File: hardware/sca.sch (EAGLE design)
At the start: 64 parts, among them IC1 BMP388, Q1 BSS138, Q2 BSS138, Q3 2N7002D, U1 MIC5225-3.3, U2 MIC5225-3.3, U5 FGPMMOPA6H, U6 MIC5225-3.3, Y1 32.768kHz

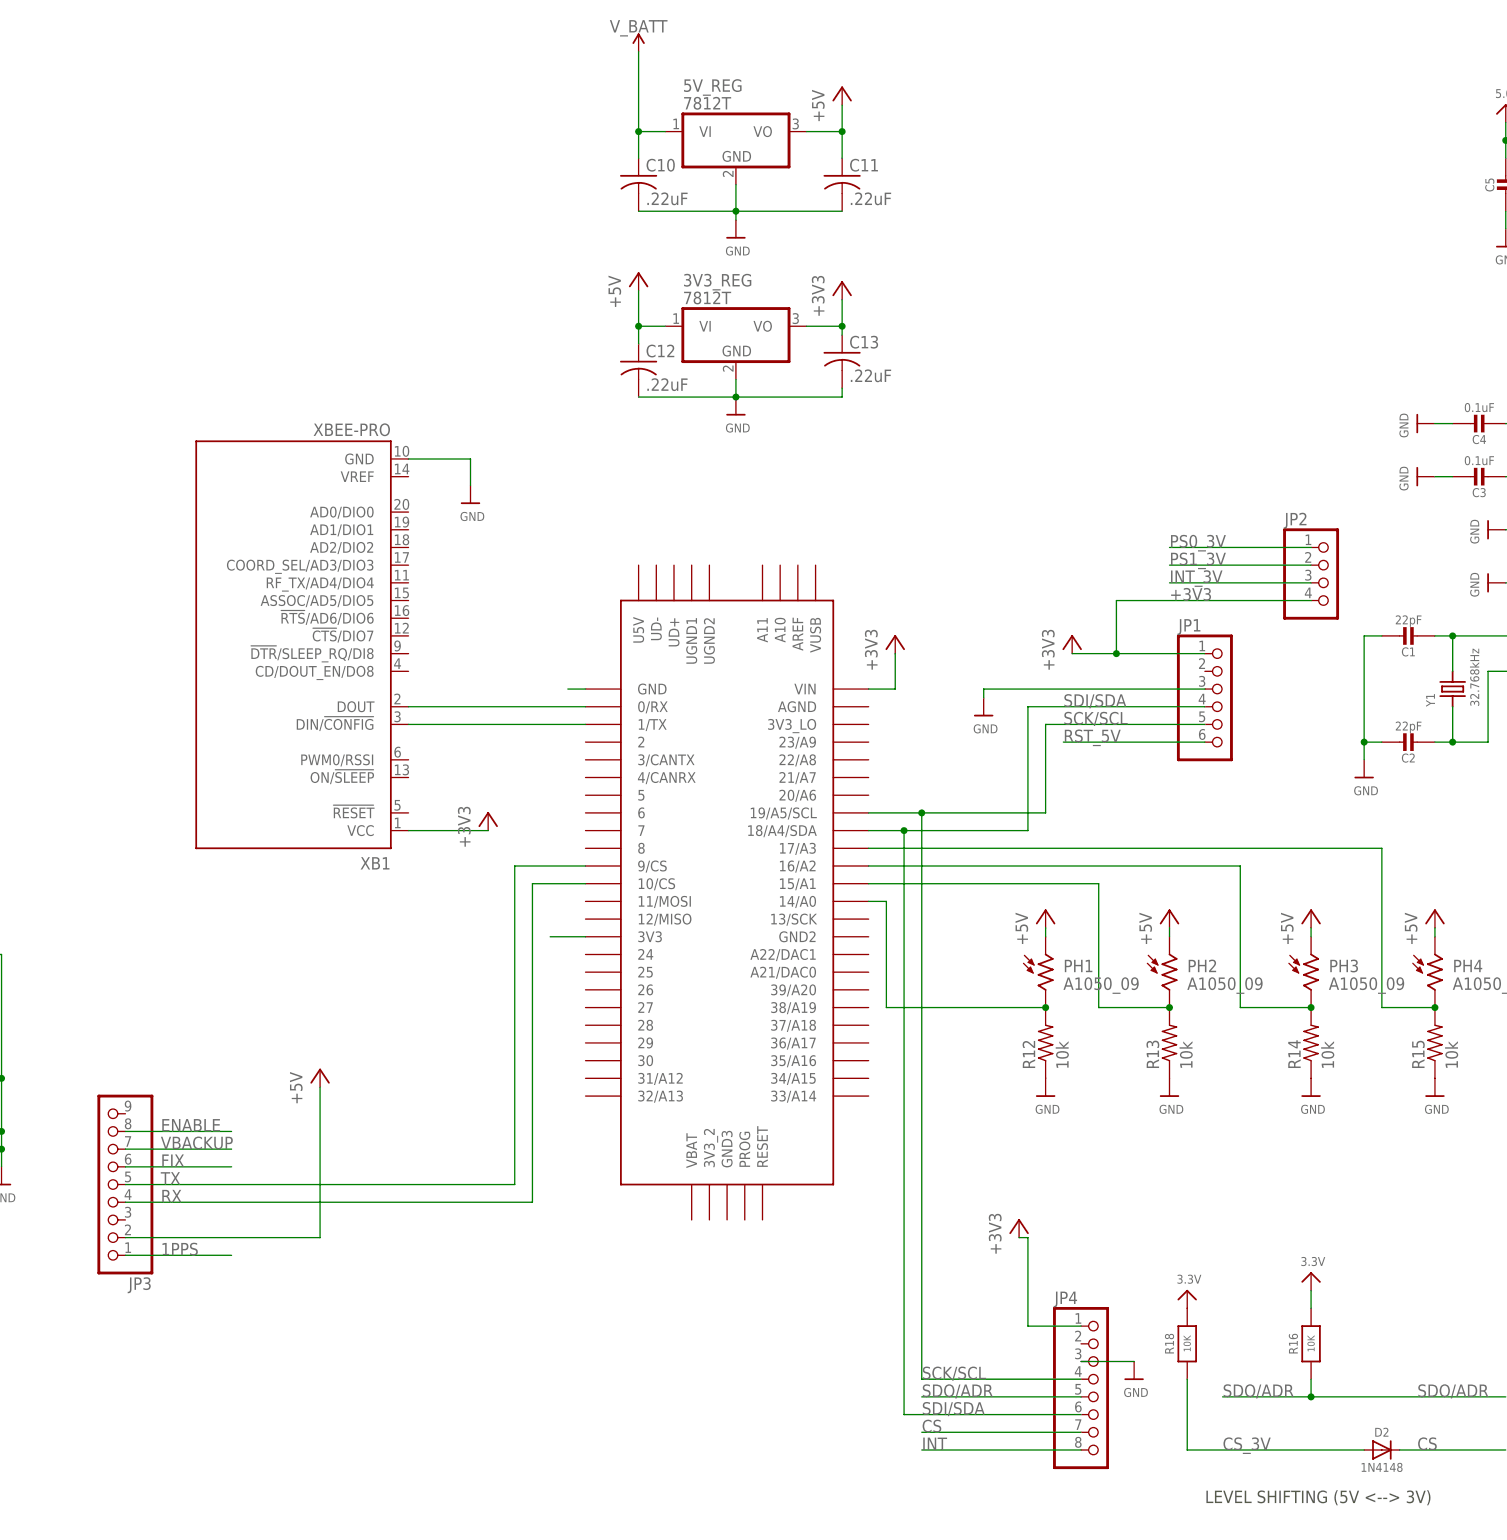
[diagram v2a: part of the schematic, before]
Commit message: added thermistor circuit
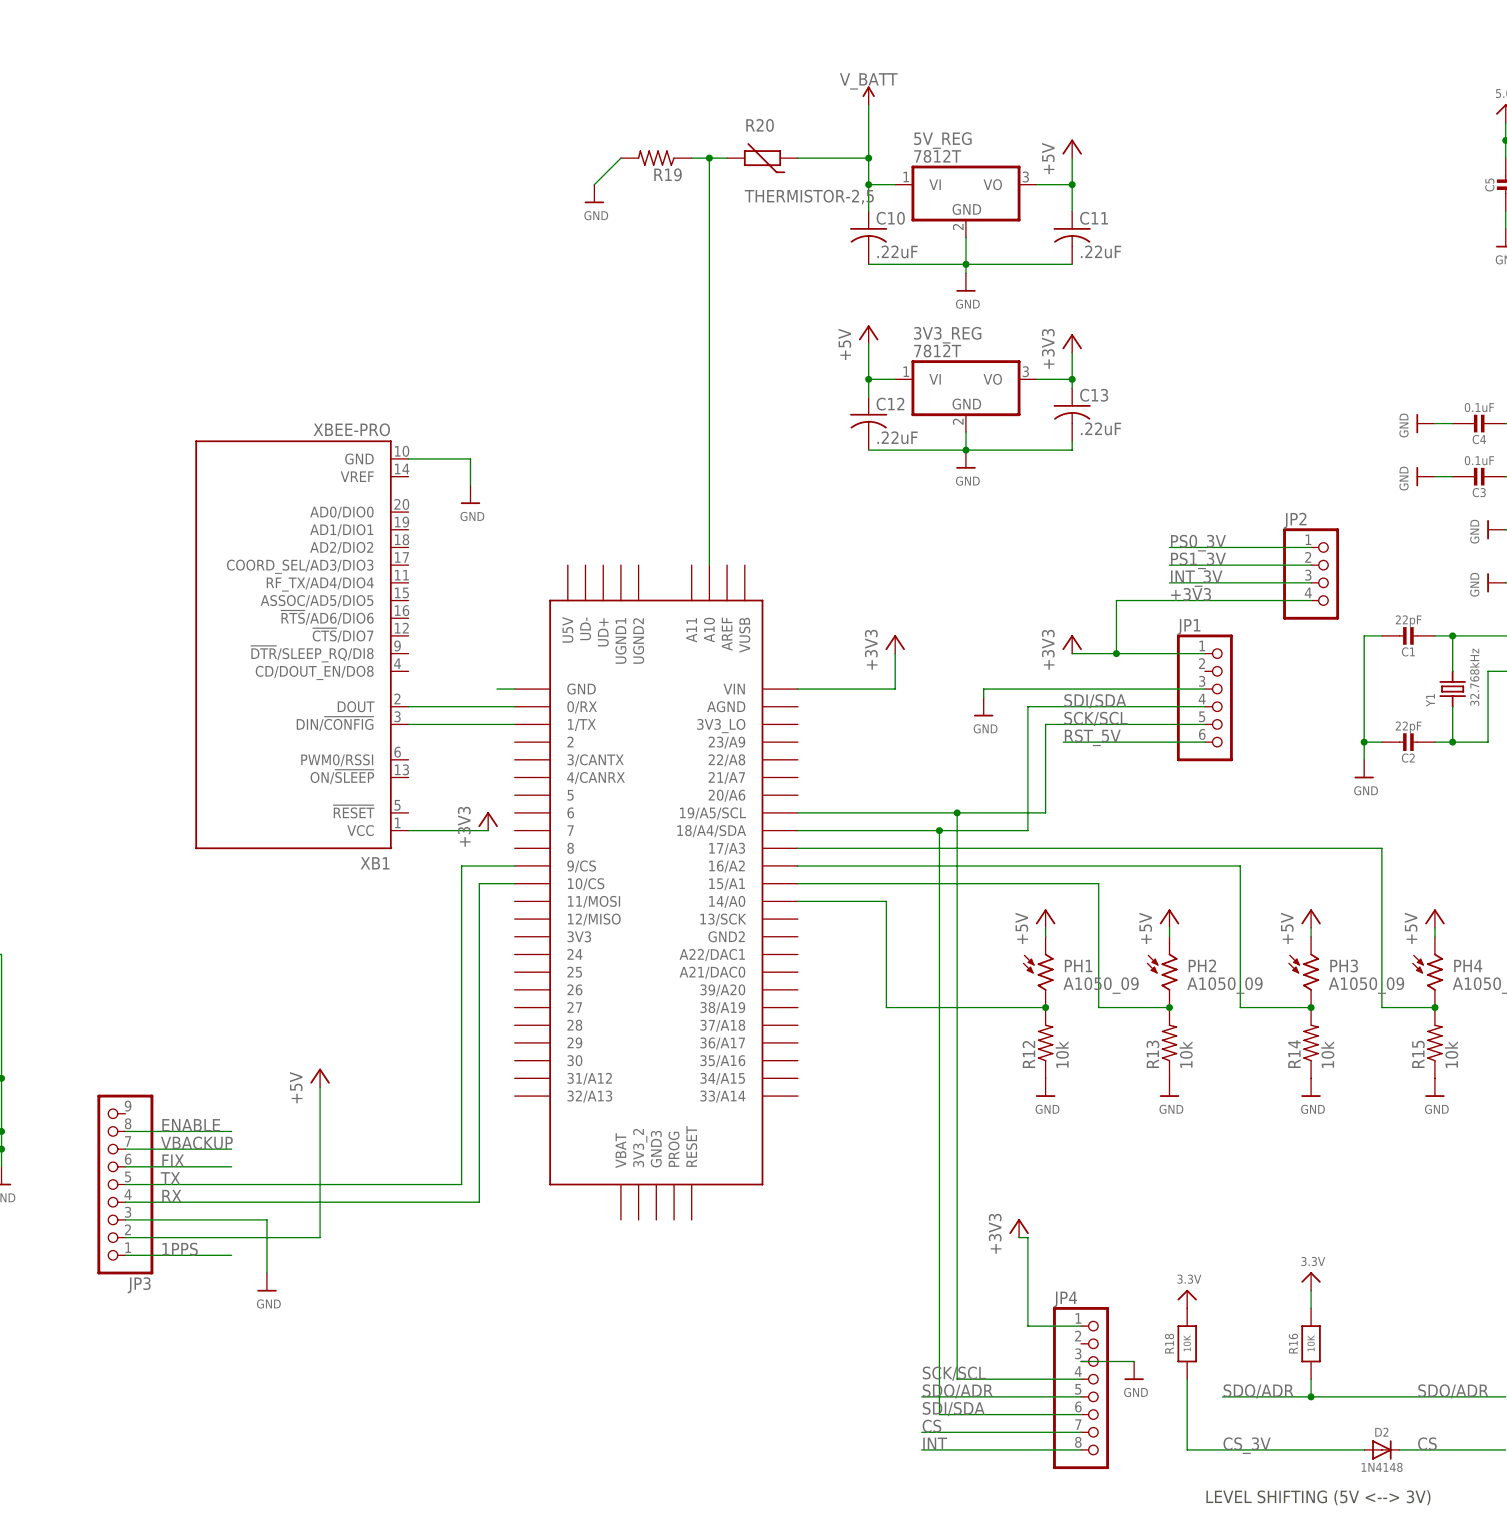
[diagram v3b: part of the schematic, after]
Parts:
- added R19: (no value), adafruit:R-US_0204/2V
- added R20: THERMISTOR-2,5, varistor:THERMISTOR-2,5
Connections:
- net GND: now also JP3.3, R19.2
- net N$9: now also R19.1, R20.2, U$1.A10; no longer U$1.3V3
- net V_BATT: now also R20.1
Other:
- moved on the sheet: 3V3_REG, 5V_REG, C10, C11, C12, C13

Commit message: Consolidated breakouts and added LEDs and battery voltage circuit
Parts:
- removed B3: CR1220, microbuilder:BATTERYCR1220_SMT
- removed C1, C2: 22pF, microbuilder:CAP_CERAMIC0805-NOOUTLINE
- removed C14, C15, C5, C8, C9: 10uF, microbuilder:CAP_CERAMIC0805-NOOUTLINE
- removed C16: 0.1uF, microbuilder:CAP_CERAMIC0603_NO
- removed C3, C7: 0.1uF, microbuilder:CAP_CERAMIC0805-NOOUTLINE
- removed C4: 0.1uF, microbuilder:CAP_CERAMIC0805_10MGAP
- removed C6: 10uF, microbuilder:CAP_CERAMIC0805_10MGAP
- removed D1: 1n4148, microbuilder:DIODESOD-323
- removed D2, D5: 1N4148, microbuilder:DIODESOD-323
- removed D6: CUS520, microbuilder:DIODESOD-323
- removed FB3: Ferrite, microbuilder:FERRITE-0805NO
- removed IC1: BMP388, microbuilder:BMP388
- removed JP1: (no value), microbuilder:HEADER-1X676MIL
- removed JP3: (no value), microbuilder:HEADER-1X970MIL
- removed Q1, Q2: BSS138, microbuilder:MOSFET-NWIDE
- removed Q3: 2N7002D, microbuilder:MOSFET-N_DUAL
- removed R10: 10K, microbuilder:RESISTOR_0805MP
- removed R11, R6, R8, R9: 10K, microbuilder:RESISTOR0805_NOOUTLINE
- removed R16, R18: 10K, microbuilder:RESISTOR_0603_NOOUT
- removed R17: 10K, microbuilder:RESISTOR_4PACK
- removed R7: 1K, microbuilder:RESISTOR0805_NOOUTLINE
- removed U$2: BNO055, microbuilder:BNO055
- removed U$49: U.FL, microbuilder:U.FL
- removed U1, U2, U6: MIC5225-3.3, microbuilder:VREG_SOT23-5
- removed U5: FGPMMOPA6H, microbuilder:GPS_FGPMMOPA6H
- removed Y1: 32.768kHz, microbuilder:CRYSTAL8.0X3.8
- added JP7: (no value), microbuilder:HEADER-1X676MIL
- added JP8: (no value), microbuilder:HEADER-1X476MIL
- added LED1, LED2: (no value), adafruit:LED3MM
- JP2: device microbuilder:HEADER-1X476MIL -> microbuilder:HEADER-1X870MIL
- JP4: device microbuilder:HEADER-1X870MIL -> microbuilder:HEADER-1X970MIL
- LED3: value RED -> (none); device microbuilder:LED0805 -> adafruit:LED3MM
- R1: value 10K -> 1M; device microbuilder:RESISTOR0805_NOOUTLINE -> resistor:R-US_0309/10
- R2: value 10K -> 1M; device microbuilder:RESISTOR_0805MP -> resistor:R-US_0309/10
- R3, R4, R5: value 10K -> 560; device microbuilder:RESISTOR0805_NOOUTLINE -> resistor:R-US_0309/10
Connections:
- removed net 3.3V: C14.1, C16.1, C4.2, C6.1, C7.1, C8.1, FB3.P$2, IC1.VDD, IC1.VDDIO, Q1.G, Q2.G, Q3G$1.G, Q3G$2.G, R1.2, R11.2, R16.2, R17G$2.1, R17G$4.1, R18.2, R6.2, R9.1, U$2.NBOOT_LOAD_PIN, U$2.VDD, U$2.VDDIO, U1.OUT, U2.OUT, U5.VCC
- removed net 5.0V: C5.1, R10.2, R2.2, U1.EN, U1.IN
- removed net CS_3V: D2.A, IC1.CSB, R18.1
- removed net N$1: U$1.GND
- removed net N$19: U$49.SIGNAL, U5.EX_ANT
- removed net N$20: B3.+, D6.A
- removed net NRESET_3V: D1.A, R11.1, U$2.NRESET
- removed net RX_3V: D5.A, R9.2, U5.RX
- removed net SCK_3V: IC1.SCK, Q3G$1.S, R17G$2.2
- removed net SCL_3V: Q2.S, R1.1, U$2.COM1/SCL/RX
- removed net SCL_5V: Q2.D, R10.1
- removed net SDA_3V: Q1.S, R6.1, U$2.COM0/SDA/TX
- removed net SDA_5V: Q1.D, R2.1
- removed net SDI_3V: IC1.SDI, Q3G$2.S, R17G$4.2
- removed net VIN: C15.1, C9.1, R17G$1.1, R17G$3.1, R8.2, U2.EN, U2.IN, U6.IN
- new net N$13: LED3.A, R5.2
- new net N$14: R5.1, U$1.30
- new net N$16: R4.1, U$1.29
- new net N$17: R3.1, U$1.28
- net +3V3: now also JP2.1, JP7.2; no longer JP1.1, JP2.4, JP4.1
- net +5V: now also JP4.2, JP7.1; no longer JP3.2
- net 1PPS: now also JP4.1; no longer JP3.1, U5.1PPS
- net CS: now also JP2.7; no longer D2.C, JP4.7
- net ENABLE: now also JP4.8; no longer JP3.8, R8.1, U6.EN
- net FIX: now also JP4.6; no longer JP3.6, LED3.A, U5.3D-FIX
- net GND: now also JP2.3, JP7.3, LED1.C, LED2.C, LED3.C, R2.2, U$1.GND; no longer B3.-, C1.1, C14.2, C15.2, C16.2, C2.1, C3.1, C4.1, C5.2, C6.2, C7.2, C8.2, C9.2, IC1.GND, JP1.3, JP3.3, R3.2, R4.2, R5.2, R7.1, U$2.COM2(GND), U$2.GND@1, U$2.GND@2, U$2.PIN10(GND), U$2.PIN15(GND), U$2.PIN16(GND), U$49.GND@0, U$49.GND@1, U1.GND, U2.GND, U5.GND@1, U5.GND@2, U5.GND@3, U5.GND@4, U6.GND
- net I2CADDR_3V: now also JP8.4; no longer R5.1, U$2.COM3/I2C_ADDR
- net INT: now also JP2.8; no longer IC1.INT, JP4.8
- net INT_3V: now also JP8.3; no longer JP2.3, U$2.INT
- net N$18: now also R1.1, R2.1, U$1.2; no longer LED3.C, R7.2
- net N$3: now also JP4.9; no longer FB3.P$1, U6.OUT
- net N$6: now also JP2.2; no longer C1.2, U$2.XIN32, Y1.2
- net N$7: now also LED1.A, R3.2; no longer C2.2, U$2.XOUT32, Y1.1
- net N$8: now also LED2.A, R4.2; no longer C3.2, U$2.CAP
- net PS0_3V: now also JP8.1; no longer JP2.1, R3.1, U$2.PS0
- net PS1_3V: now also JP8.2; no longer JP2.2, R4.1, U$2.PS1
- net RST_5V: now also JP7.6; no longer D1.C, JP1.6
- net RX: now also JP4.4; no longer D5.C, JP3.4
- net SCK/SCL: now also JP2.4, JP7.5; no longer JP1.5, JP4.4, Q3G$1.D, R17G$1.2
- net SDI/SDA: now also JP2.6, JP7.4; no longer JP1.4, JP4.6, Q3G$2.D, R17G$3.2
- net SDO/ADR: now also JP2.5; no longer IC1.SDO, JP4.5, R16.1
- net TX: now also JP4.5; no longer JP3.5, U5.TX
- net VBACKUP: now also JP4.7; no longer D6.C, JP3.7, U5.VBACKUP
- net V_BATT: now also R1.2
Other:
- note removed: "D"
- note removed: "D1+R3 restrict RX input to 3.3V"
- note removed: "For I2C leave CSB pulled high (default value) SDI=SDA, SCK=SCL"
- note removed: "For SPI set CSB low at startup SDO=MISO, SDI=MOSI, SCK=SCK, CSB=CS/SSEL"
- note removed: "G"
- note removed: "LEVEL SHIFTING (5V <--> 3V)"
- note removed: "S"
- moved on the sheet: C10, C11, C12, C13, PH1, PH2, PH3, PH4, R12, R13, R14, R15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

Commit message: added frame and cleaned up
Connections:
- removed net N$6 (its old number): JP2.2
- removed net SDO/ADR: JP2.5
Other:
- note added: "University of Pittsburgh SOAR Avionics Team 2019 - 2020 NASA Student Launch"
- moved on the sheet: C10, C11, C12, C13, JP2, JP4, JP7, JP8, LED1, LED2, LED3, PH1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

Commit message: forgot to save last time
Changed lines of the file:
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@@
 <attribute name="VALUE" x="135.89" y="7.62" size="1.778" layer="96"/>
 </instance>
-<instance part="+3V3" gate="G$1" x="133.35" y="38.1" smashed="yes" grouprefs="BMP338">
-<attribute name="VALUE" x="135.89" y="40.64" size="1.778" layer="96" rot="R180"/>
+<instance part="+3V3" gate="G$1" x="130.81" y="38.1" smashed="yes" grouprefs="BMP338">
+<attribute name="VALUE" x="133.35" y="40.64" size="1.778" layer="96" rot="R180"/>
 </instance>
 <instance part="U$7" gate="G$1" x="40.64" y="22.86" smashed="yes" grouprefs="GPS">
@@
 </segment>
 <segment>
-<wire x1="139.7" y1="30.48" x2="133.35" y2="30.48" width="0.1524" layer="91" grouprefs="BMP338"/>
+<wire x1="139.7" y1="30.48" x2="130.81" y2="30.48" width="0.1524" layer="91" grouprefs="BMP338"/>
 <pinref part="JP2" gate="A" pin="1"/>
 <pinref part="+3V3" gate="G$1" pin="+3V3"/>
-<wire x1="133.35" y1="35.56" x2="133.35" y2="30.48" width="0.1524" layer="91" grouprefs="BMP338"/>
-</segment>
-</net>
+<wire x1="130.81" y1="35.56" x2="130.81" y2="30.48" width="0.1524" layer="91" grouprefs="BMP338"/>
+</segment>
+</net>

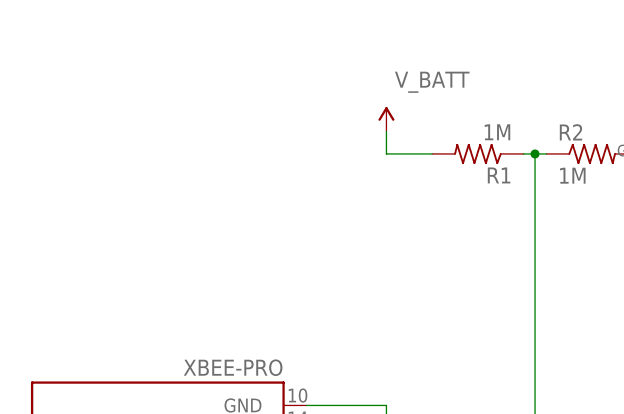
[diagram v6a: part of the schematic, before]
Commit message: added XT60 connector
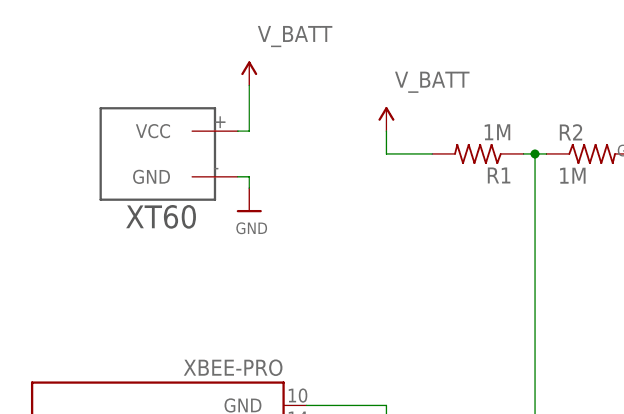
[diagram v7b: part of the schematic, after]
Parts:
- added U$5: XT60, XT60:XT60
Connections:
- net GND: now also U$5.GND
- net V_BATT: now also U$5.VCC
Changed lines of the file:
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@@
 <part name="SUPPLY1" library="SparkFun-PowerSymbols" library_urn="urn:adsk.eagle:library:530" deviceset="V_BATT" device=""/>
 <part name="FRAME1" library="frames" library_urn="urn:adsk.eagle:library:229" deviceset="A4L-LOC" device=""/>
+<part name="U$5" library="XT60" deviceset="XT60" device=""/>
+<part name="SUPPLY3" library="SparkFun-PowerSymbols" library_urn="urn:adsk.eagle:library:530" deviceset="V_BATT" device=""/>
+<part name="U$8" library="microbuilder" deviceset="GND" device=""/>
 </parts>
 <sheets>
@@
 <attribute name="SHEET" x="230.505" y="5.08" size="2.54" layer="94"/>
 </instance>
+<instance part="U$5" gate="G$1" x="30.48" y="157.48" smashed="yes" rot="R180"/>
+<instance part="SUPPLY3" gate="G$1" x="36.83" y="165.1" smashed="yes">
+<attribute name="VALUE" x="41.91" y="171.704" size="1.778" layer="96" rot="R180" align="bottom-center"/>
+</instance>
+<instance part="U$8" gate="G$1" x="36.83" y="151.13" smashed="yes">
+<attribute name="VALUE" x="35.306" y="148.59" size="1.27" layer="96"/>
+</instance>
 </instances>
 <busses>
@@
 <junction x="99.06" y="15.24"/>
 </segment>
+<segment>
+<pinref part="U$5" gate="G$1" pin="GND"/>
+<pinref part="U$8" gate="G$1" pin="GND"/>
+<wire x1="35.56" y1="154.94" x2="36.83" y2="154.94" width="0.1524" layer="91"/>
+<wire x1="36.83" y1="154.94" x2="36.83" y2="153.67" width="0.1524" layer="91"/>
+</segment>
 </net>
 <net name="ENABLE" class="0">
@@
 <wire x1="52.07" y1="157.48" x2="52.07" y2="160.02" width="0.1524" layer="91"/>
 </segment>
-</net>
+<segment>
+<pinref part="U$5" gate="G$1" pin="VCC"/>
+<pinref part="SUPPLY3" gate="G$1" pin="V_BATT"/>
+<wire x1="35.56" y1="160.02" x2="36.83" y2="160.02" width="0.1524" layer="91"/>
+<wire x1="36.83" y1="160.02" x2="36.83" y2="165.1" width="0.1524" layer="91"/>
+</segment>
+</net>
